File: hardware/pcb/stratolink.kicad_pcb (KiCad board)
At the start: 2 copper layers, 23.4 x 57.3 mm, 59 parts, among them J1 Solar panel direct solder, J2 Solar panel direct solder, J20 Conn_ARM_SWD_TagConnect_TC203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, J3 Conn_PinHeader_1x07_P2.54mm_V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, J4 Conn_PinHeader_1x07_P2.54mm_V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, U2 RAK3172, U5 TMP117NAIYBGR, U7 LIS2DH12TR

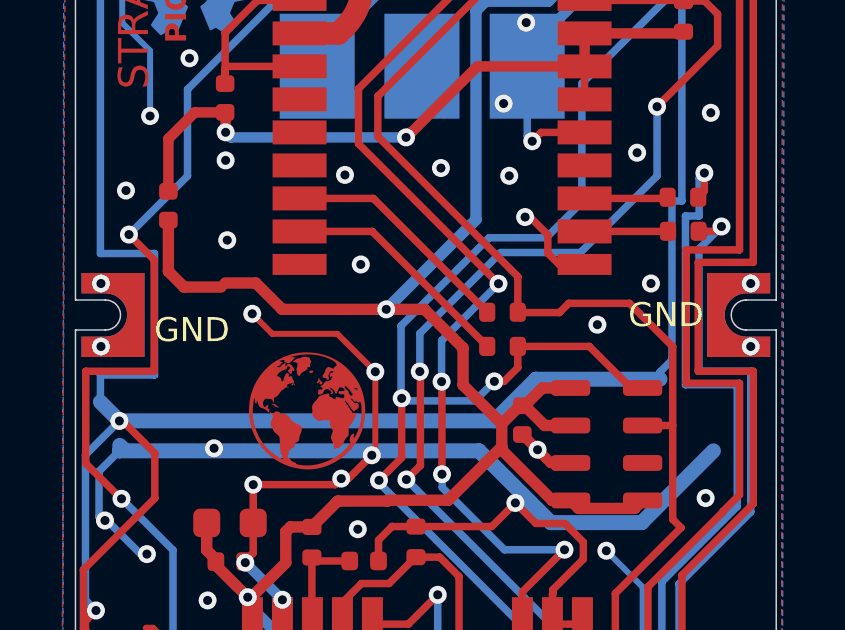
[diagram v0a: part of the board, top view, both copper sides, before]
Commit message: Refine solar notches and scale assembly from ZachTek photo
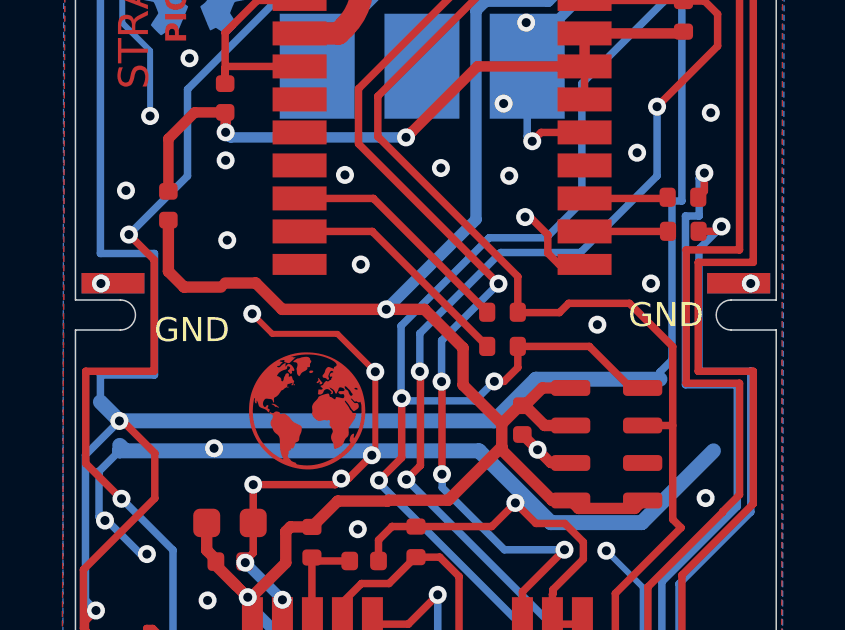
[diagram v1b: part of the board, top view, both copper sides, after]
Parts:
- J1: footprint lib:Solar_Notch_Right_1p0x1p5 -> lib:Solar_Notch_Right_1p0x2p0
- J2: footprint lib:Solar_Notch_Left_1p0x1p5 -> lib:Solar_Notch_Left_1p0x2p0
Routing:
- net GND: vias 87 -> 85
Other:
- outline, holes or cut-outs redrawn

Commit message: Improve suspension corners with plated holes and reviewed load models
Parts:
- added H1: Suspension 2.0 mm PTH, lib:Suspension_PTH_D2p0_OD3p2, F.Cu at (55.7, 31.7)
- added H2: Suspension 2.0 mm PTH, lib:Suspension_PTH_D2p0_OD3p2, F.Cu at (74.3, 31.7)
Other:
- outline, holes or cut-outs redrawn
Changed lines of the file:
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@@
 		)
 	)
+	(footprint "lib:Suspension_PTH_D2p0_OD3p2"
+		(layer "F.Cu")
+		(at 74.327 31.745)
+		(descr "Manual string suspension: 2.0 mm finished plated hole, 3.2 mm GND pad, solid zone connection")
+		(property "Reference" "H2"
+			(at 0 -2.3 0)
+			(layer "F.Fab")
+			(hide yes)
+			(effects
+				(font
+					(size 0.7 0.7)
+					(thickness 0.1)
+				)
+			)
+		)
+		(property "Value" "Suspension 2.0 mm PTH"
+			(at 0 2.3 0)
+			(layer "F.Fab")
+			(hide yes)
+			(effects
+				(font
+					(size 0.7 0.7)
+					(thickness 0.1)
+				)
+			)
+		)
+		(property "Datasheet" ""
+			(at 0 0 0)
+			(layer "F.Fab")
+			(hide yes)
+			(effects
+				(font
+					(size 1.27 1.27)
+				)
+			)
+		)
+		(property "Description" ""
+			(at 0 0 0)
+			(layer "F.Fab")
+			(hide yes)
+			(effects
+				(font
+					(size 1.27 1.27)
+				)
+			)
+		)
+		(attr through_hole board_only exclude_from_pos_files exclude_from_bom)
+		(duplicate_pad_numbers_are_jumpers no)
+		(fp_circle
+			(center 0 0)
+			(end 1.85 0)
+			(stroke
+				(width 0.05)
+				(type solid)
+			)
+			(fill no)
+			(layer "B.CrtYd")
+		)
+		(fp_circle
+			(center 0 0)
+			(end 1.85 0)
+			(stroke
+				(width 0.05)
+				(type solid)
+			)
+			(fill no)
+			(layer "F.CrtYd")
+		)
+		(pad "1" thru_hole circle
+			(at 0 0)
+			(size 3.2 3.2)
+			(drill 2)
+			(layers "*.Cu" "*.Mask")
+			(remove_unused_layers no)
+			(net "GND")
+			(zone_connect 2)
+		)
+		(embedded_fonts no)
+	)
 	(footprint "lib:4269"
 		(layer "F.Cu")
@@
 		)
 	)
+	(footprint "lib:Suspension_PTH_D2p0_OD3p2"
+		(layer "F.Cu")
+		(at 55.665 31.745)
+		(descr "Manual string suspension: 2.0 mm finished plated hole, 3.2 mm GND pad, solid zone connection")
+		(property "Reference" "H1"
+			(at 0 -2.3 0)
+			(layer "F.Fab")
+			(hide yes)
+			(effects
+				(font
+					(size 0.7 0.7)
+					(thickness 0.1)
+				)
+			)
+		)
+		(property "Value" "Suspension 2.0 mm PTH"
+			(at 0 2.3 0)
+			(layer "F.Fab")
+			(hide yes)
+			(effects
+				(font
+					(size 0.7 0.7)
+					(thickness 0.1)
+				)
+			)
+		)
+		(property "Datasheet" ""
+			(at 0 0 0)
+			(layer "F.Fab")
+			(hide yes)
+			(effects
+				(font
+					(size 1.27 1.27)
+				)
+			)
+		)
+		(property "Description" ""
+			(at 0 0 0)
+			(layer "F.Fab")
+			(hide yes)
+			(effects
+				(font
+					(size 1.27 1.27)
+				)
+			)
+		)
+		(attr through_hole board_only exclude_from_pos_files exclude_from_bom)
+		(duplicate_pad_numbers_are_jumpers no)
+		(fp_circle
+			(center 0 0)
+			(end 1.85 0)
+			(stroke
+				(width 0.05)
+				(type solid)
+			)
+			(fill no)
+			(layer "B.CrtYd")
+		)
+		(fp_circle
+			(center 0 0)
+			(end 1.85 0)
+			(stroke
+				(width 0.05)
+				(type solid)
+			)
+			(fill no)
+			(layer "F.CrtYd")
+		)
+		(pad "1" thru_hole circle
+			(at 0 0)
+			(size 3.2 3.2)
+			(drill 2)
+			(layers "*.Cu" "*.Mask")
+			(remove_unused_layers no)
+			(net "GND")
+			(zone_connect 2)
+		)
+		(embedded_fonts no)
+	)
 	(footprint "Diode_SMD:D_SOD-523"
 		(layer "F.Cu")
@@
 		(layer "Edge.Cuts")
 	)
-	(gr_circle
-		(center 55.665 31.745)
-		(end 57.015 31.708)
-		(stroke
-			(width 0.05)
-			(type default)
-		)
-		(fill no)
-		(layer "Edge.Cuts")
-	)
 	(gr_arc
 		(start 55.821 86.695)
@@
 		(layer "Edge.Cuts")
 	)
-	(gr_circle
-		(center 74.327 31.745)
-		(end 75.677 31.708)
-		(stroke
-			(width 0.05)
-			(type default)
-		)
-		(fill no)
-		(layer "Edge.Cuts")
-	)
